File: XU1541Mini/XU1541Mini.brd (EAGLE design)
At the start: 49.5 x 49.5 mm, 20 parts, among them IC1 ATmega8, Q1 12MHz

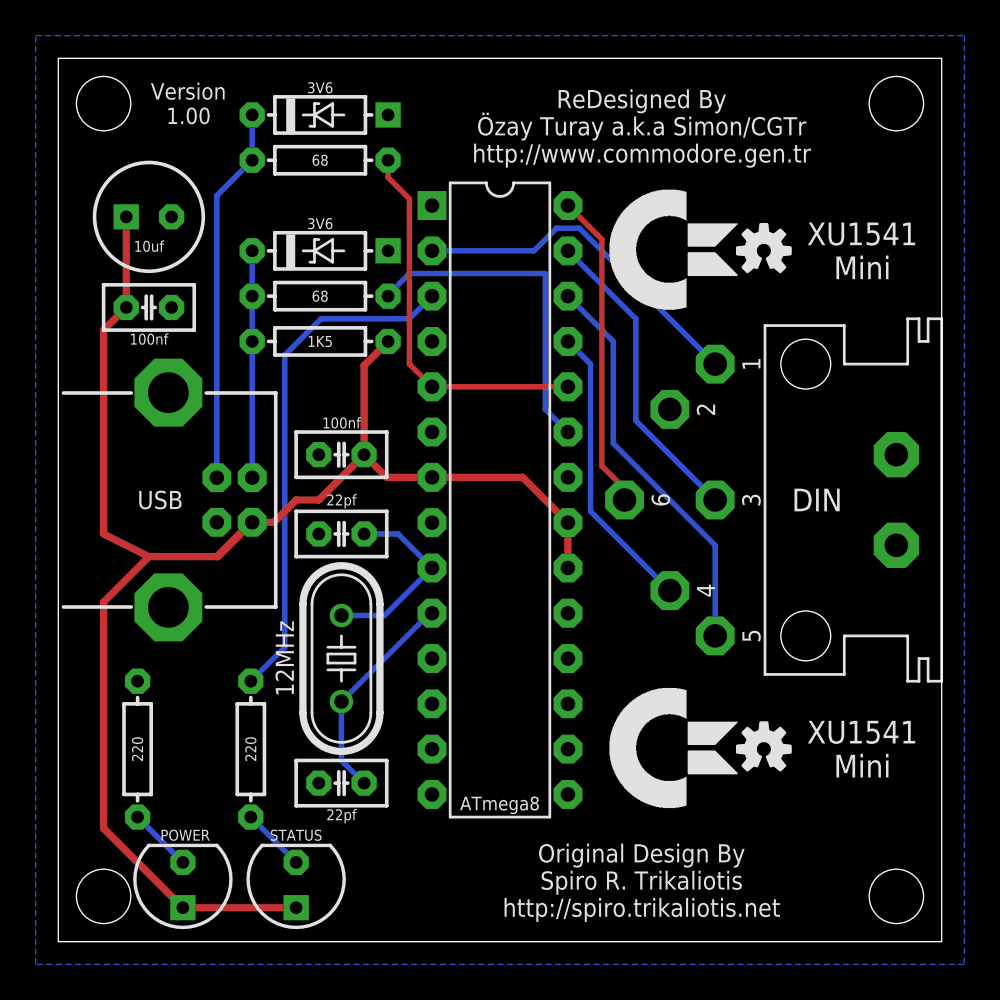
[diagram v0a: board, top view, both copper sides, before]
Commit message: Updated project files and added missing preview images
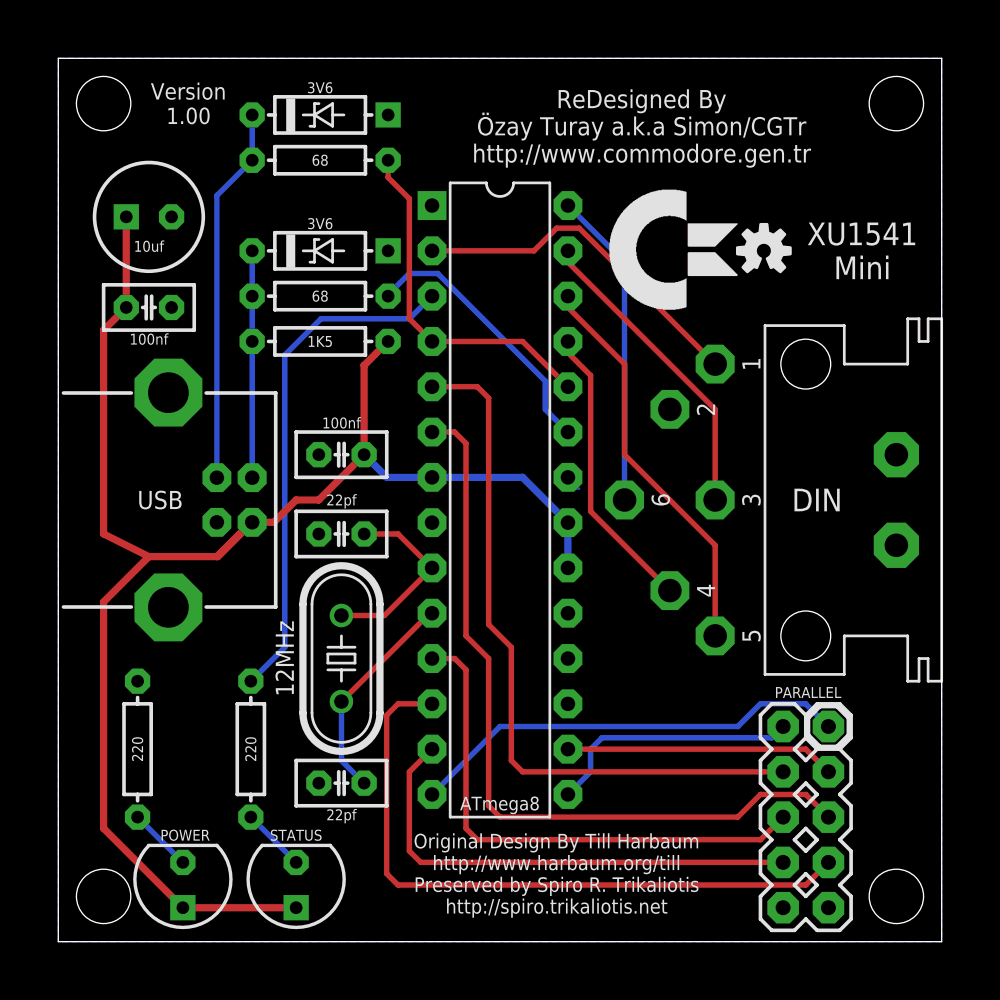
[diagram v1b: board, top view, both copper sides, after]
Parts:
- removed LOGO2: OSHW_LOGO_SMALL, sj_standart:OSHW_LOGO_SMALL
- added JP1: PARALLEL, sj_connectors:HDR_2X05
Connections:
- new net N$1: IC1.14, JP1.1
- new net N$2: IC1.15, JP1.2
- new net N$3: IC1.16, JP1.3
- new net N$4: IC1.5, JP1.4
- new net N$5: IC1.6, JP1.5
- new net N$6: IC1.11, JP1.6
- new net N$7: IC1.12, JP1.7
- new net N$8: IC1.13, JP1.8
- net D+@2: now also IC1.4; no longer IC1.5
- net GND: now also JP1.10, JP1.9
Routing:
- net N$5: track 0.00 -> 43.4 mm
- net N$4: track 0.00 -> 39.8 mm
- net N$7: track 0.00 -> 37.2 mm
- net N$6: track 0.00 -> 29.6 mm
- net N$8: track 0.00 -> 27.5 mm
- net N$1: track 0.00 -> 24.9 mm
- net N$3: track 0.00 -> 15.1 mm
- net N$2: track 0.00 -> 14.4 mm
- net D-@2: track 18.8 -> 15.3 mm
- net D+@2: track 21.3 -> 19.9 mm
- net GND: track 0.00 -> 0.63 mm
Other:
- board text added: "Original Design By Till Harbaum http://www.harbaum.org/till Preserved by Spiro R. Trikaliotis http://spiro.trikaliotis.net"
- board text removed: "Original Design By Spiro R. Trikaliotis http://spiro.trikaliotis.net"
